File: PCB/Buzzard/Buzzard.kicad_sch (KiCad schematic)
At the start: 71 parts, among them J1 PJ-320A, J4 Haptic Buzz, J5 TrackPoint, J6 OLED, J7 Sharp Memory LCD Breakout, J8 Battery, SW1 SW_DPST_x2, SW2 Reset, U1 ProMicro

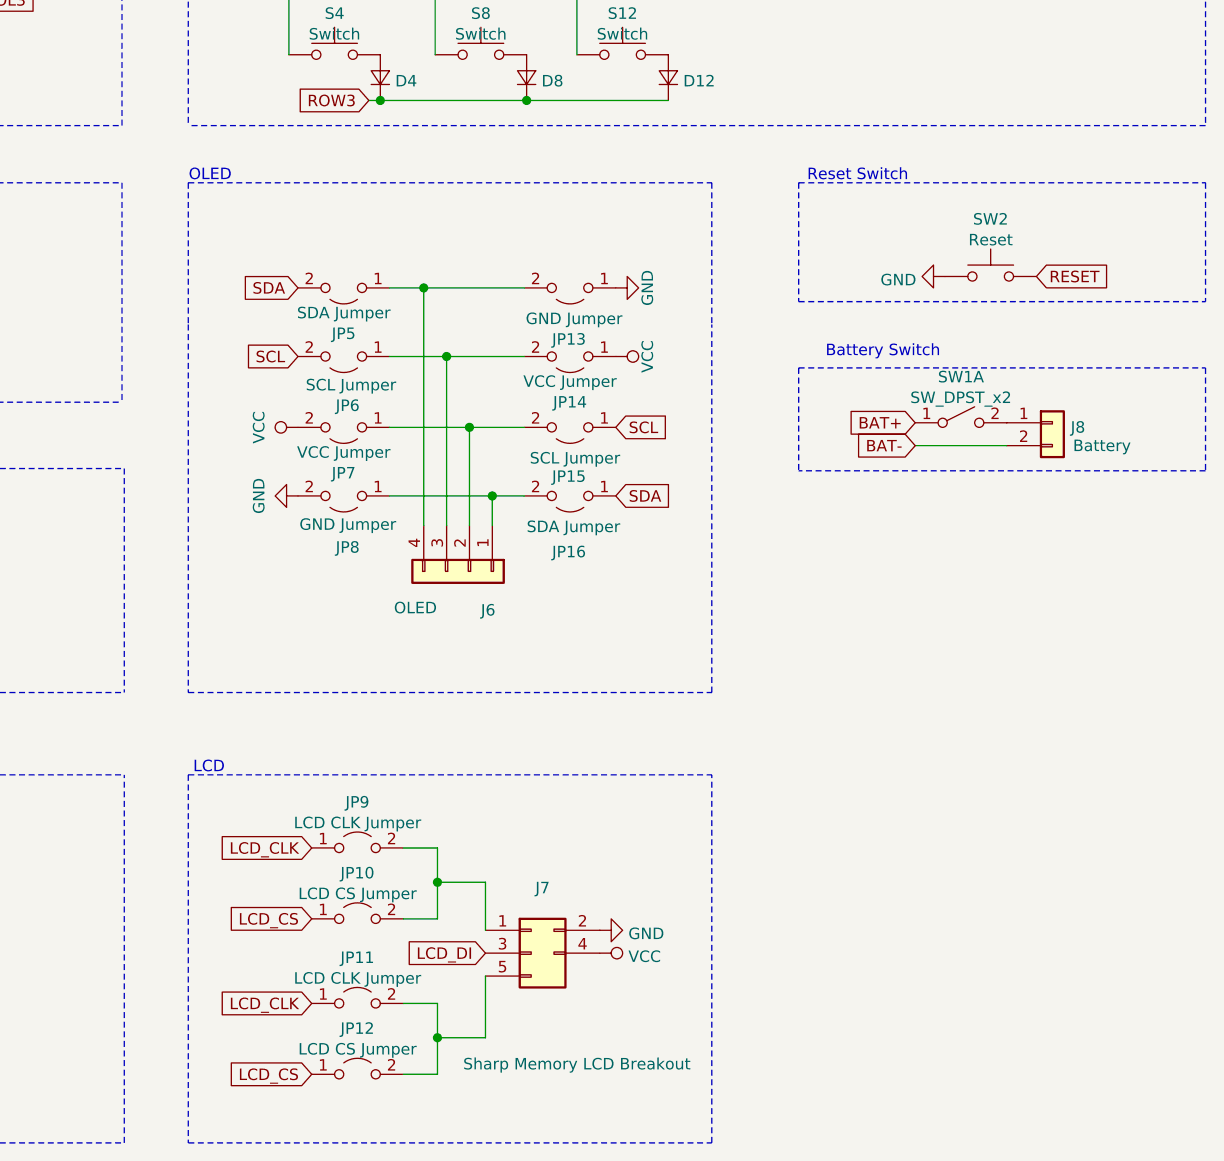
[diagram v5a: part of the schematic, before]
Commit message: replaced lcd footprint and fixed connections
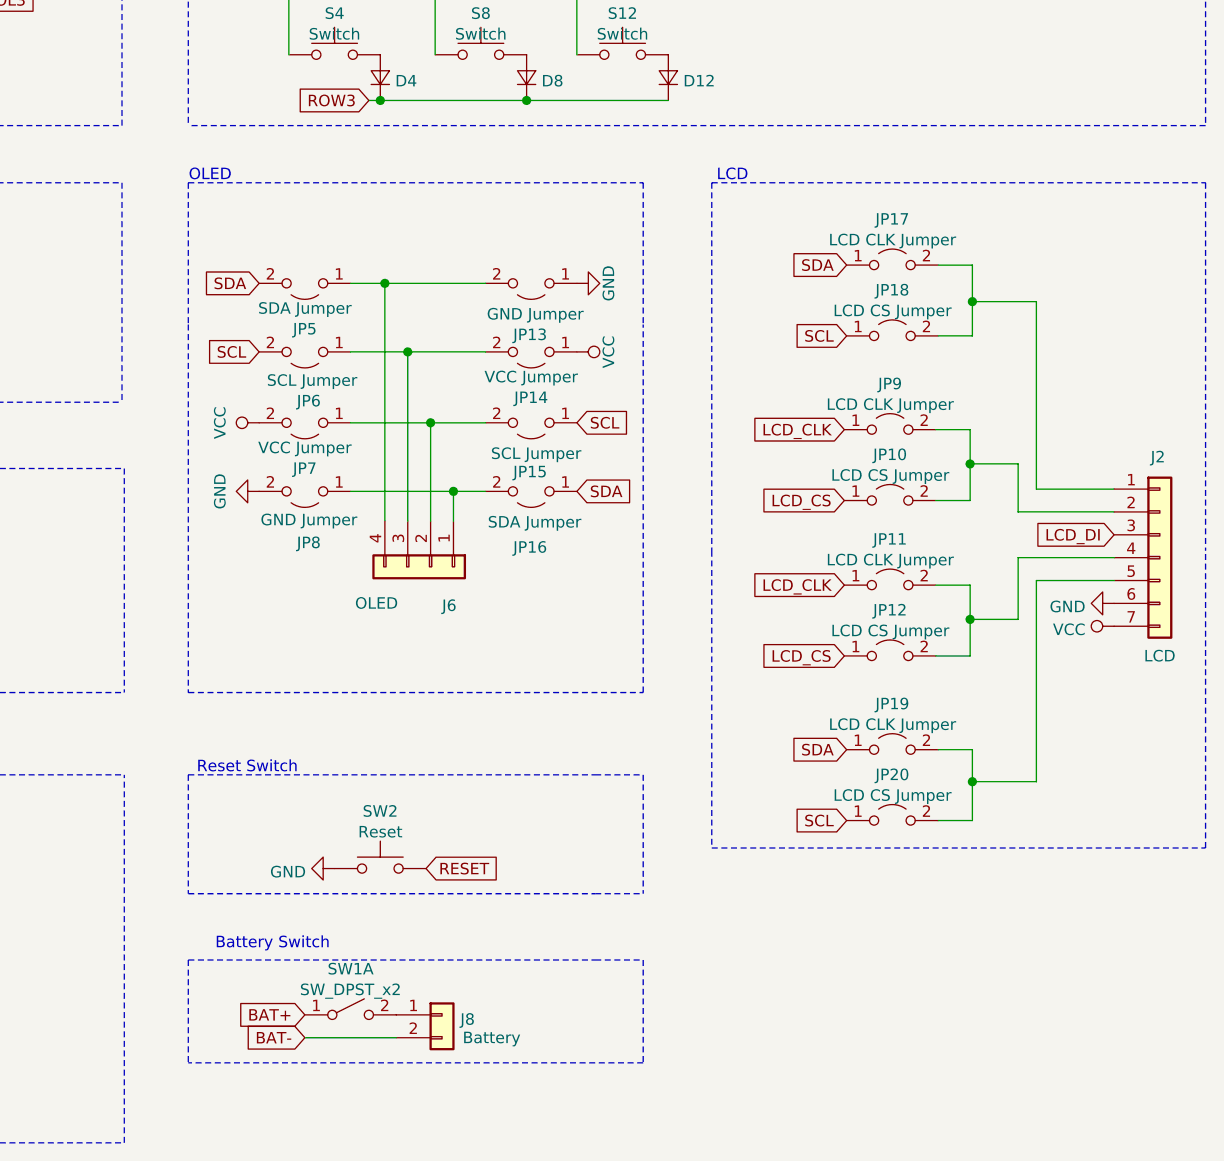
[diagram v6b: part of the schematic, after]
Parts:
- removed J7: Sharp Memory LCD Breakout, Buzzard:SharpMemoryLcdBreakout-Reversable, symbol Connector_Generic:Conn_2Rows-05Pins
- added J2: LCD, Buzzard:SharpMemoryLcdBreakout-Reversable, symbol Connector_Generic:Conn_01x07
- added JP17, JP19: LCD CLK Jumper, Jumper:SolderJumper-2_P1.3mm_Open_Pad1.0x1.5mm, symbol Jumper:Jumper_2_Open
- added JP18, JP20: LCD CS Jumper, Jumper:SolderJumper-2_P1.3mm_Open_Pad1.0x1.5mm, symbol Jumper:Jumper_2_Open
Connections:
- net GND: now also J2.6 (Pin_6)
- net LCD_DI: now also J2.3 (Pin_3)
- net SCL: now also JP18.1 (A), JP20.1 (A)
- net SDA: now also JP17.1 (A), JP19.1 (A)
- net VCC: now also J2.7 (Pin_7)
- net at JP11.2 (B), JP12.2 (B): now also J2.4 (Pin_4)
- net at JP10.2 (B), JP9.2 (B): now also J2.2 (Pin_2)
- new net: J2.1 (Pin_1), JP17.2 (B), JP18.2 (B)
- new net: J2.5 (Pin_5), JP19.2 (B), JP20.2 (B)
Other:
- moved on the sheet: J6, J8, JP10, JP11, JP12, JP13, JP14, JP15, JP16, JP5, JP6, JP7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

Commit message: added mounting holes
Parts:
- added U2, U3: Hole, Buzzard:M2_HOLE_PCB, symbol Buzzard:Hole
- added U4, U5, U6, U7, U8, U9, U? (x4): Hole, Buzzard:HOLE_M2_TH, symbol Buzzard:Hole
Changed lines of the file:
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@@
     (pin "2")
+  )
+  (symbol (lib_id "Buzzard:Hole") (at 240.538 70.612 0) (unit 1)
+    (in_bom yes) (on_board yes) (fields_autoplaced)
+    (property "Reference" "U5" (id 0) (at 244.9831 69.0894 0)
+      (effects (font (size 1.524 1.524)) (justify left))
+    )
+    (property "Value" "Hole" (id 1) (at 244.9831 71.797 0)
+      (effects (font (size 1.524 1.524)) (justify left))
+    )
+    (property "Footprint" "Buzzard:HOLE_M2_TH" (id 2) (at 240.538 70.612 0)
+      (effects (font (size 1.524 1.524)) hide)
+    )
+    (property "Datasheet" "" (id 3) (at 240.538 70.612 0)
+      (effects (font (size 1.524 1.524)))
+    )
+  )
+  (symbol (lib_id "Buzzard:Hole") (at 242.57 116.586 0) (unit 1)
+    (in_bom yes) (on_board yes) (fields_autoplaced)
+    (property "Reference" "U?" (id 0) (at 247.0151 115.0634 0)
+      (effects (font (size 1.524 1.524)) (justify left))
+    )
+    (property "Value" "Hole" (id 1) (at 247.0151 117.771 0)
+      (effects (font (size 1.524 1.524)) (justify left))
+    )
+    (property "Footprint" "Buzzard:HOLE_M2_TH" (id 2) (at 242.57 116.586 0)
+      (effects (font (size 1.524 1.524)) hide)
+    )
+    (property "Datasheet" "" (id 3) (at 242.57 116.586 0)
+      (effects (font (size 1.524 1.524)))
+    )
+  )
+  (symbol (lib_id "Buzzard:Hole") (at 242.824 102.108 0) (unit 1)
+    (in_bom yes) (on_board yes) (fields_autoplaced)
+    (property "Reference" "U?" (id 0) (at 247.2691 100.5854 0)
+      (effects (font (size 1.524 1.524)) (justify left))
+    )
+    (property "Value" "Hole" (id 1) (at 247.2691 103.293 0)
+      (effects (font (size 1.524 1.524)) (justify left))
+    )
+    (property "Footprint" "Buzzard:HOLE_M2_TH" (id 2) (at 242.824 102.108 0)
+      (effects (font (size 1.524 1.524)) hide)
+    )
+    (property "Datasheet" "" (id 3) (at 242.824 102.108 0)
+      (effects (font (size 1.524 1.524)))
+    )
+  )
+  (symbol (lib_id "Buzzard:Hole") (at 243.586 24.384 0) (unit 1)
+    (in_bom yes) (on_board yes) (fields_autoplaced)
+    (property "Reference" "U2" (id 0) (at 248.0311 22.8614 0)
+      (effects (font (size 1.524 1.524)) (justify left))
+    )
+    (property "Value" "Hole" (id 1) (at 248.0311 25.569 0)
+      (effects (font (size 1.524 1.524)) (justify left))
+    )
+    (property "Footprint" "Buzzard:M2_HOLE_PCB" (id 2) (at 243.586 24.384 0)
+      (effects (font (size 1.524 1.524)) hide)
+    )
+    (property "Datasheet" "" (id 3) (at 243.586 24.384 0)
+      (effects (font (size 1.524 1.524)))
+    )
+  )
+  (symbol (lib_id "Buzzard:Hole") (at 243.84 44.704 0) (unit 1)
+    (in_bom yes) (on_board yes) (fields_autoplaced)
+    (property "Reference" "U4" (id 0) (at 248.2851 43.1814 0)
+      (effects (font (size 1.524 1.524)) (justify left))
+    )
+    (property "Value" "Hole" (id 1) (at 248.2851 45.889 0)
+      (effects (font (size 1.524 1.524)) (justify left))
+    )
+    (property "Footprint" "Buzzard:HOLE_M2_TH" (id 2) (at 243.84 44.704 0)
+      (effects (font (size 1.524 1.524)) hide)
+    )
+    (property "Datasheet" "" (id 3) (at 243.84 44.704 0)
+      (effects (font (size 1.524 1.524)))
+    )
+  )
+  (symbol (lib_id "Buzzard:Hole") (at 259.08 70.358 0) (unit 1)
+    (in_bom yes) (on_board yes) (fields_autoplaced)
+    (property "Reference" "U7" (id 0) (at 263.5251 68.8354 0)
+      (effects (font (size 1.524 1.524)) (justify left))
+    )
+    (property "Value" "Hole" (id 1) (at 263.5251 71.543 0)
+      (effects (font (size 1.524 1.524)) (justify left))
+    )
+    (property "Footprint" "Buzzard:HOLE_M2_TH" (id 2) (at 259.08 70.358 0)
+      (effects (font (size 1.524 1.524)) hide)
+    )
+    (property "Datasheet" "" (id 3) (at 259.08 70.358 0)
+      (effects (font (size 1.524 1.524)))
+    )
+  )
+  (symbol (lib_id "Buzzard:Hole") (at 259.842 24.384 0) (unit 1)
+    (in_bom yes) (on_board yes) (fields_autoplaced)
+    (property "Reference" "U3" (id 0) (at 264.2871 22.8614 0)
+      (effects (font (size 1.524 1.524)) (justify left))
+    )
+    (property "Value" "Hole" (id 1) (at 264.2871 25.569 0)
+      (effects (font (size 1.524 1.524)) (justify left))
+    )
+    (property "Footprint" "Buzzard:M2_HOLE_PCB" (id 2) (at 259.842 24.384 0)
+      (effects (font (size 1.524 1.524)) hide)
+    )
+    (property "Datasheet" "" (id 3) (at 259.842 24.384 0)
+      (effects (font (size 1.524 1.524)))
+    )
+  )
+  (symbol (lib_id "Buzzard:Hole") (at 259.842 44.704 0) (unit 1)
+    (in_bom yes) (on_board yes) (fields_autoplaced)
+    (property "Reference" "U6" (id 0) (at 264.2871 43.1814 0)
+      (effects (font (size 1.524 1.524)) (justify left))
+    )
+    (property "Value" "Hole" (id 1) (at 264.2871 45.889 0)
+      (effects (font (size 1.524 1.524)) (justify left))
+    )
+    (property "Footprint" "Buzzard:HOLE_M2_TH" (id 2) (at 259.842 44.704 0)
+      (effects (font (size 1.524 1.524)) hide)
+    )
+    (property "Datasheet" "" (id 3) (at 259.842 44.704 0)
+      (effects (font (size 1.524 1.524)))
+    )
+  )
+  (symbol (lib_id "Buzzard:Hole") (at 261.366 101.092 0) (unit 1)
+    (in_bom yes) (on_board yes) (fields_autoplaced)
+    (property "Reference" "U?" (id 0) (at 265.8111 99.5694 0)
+      (effects (font (size 1.524 1.524)) (justify left))
+    )
+    (property "Value" "Hole" (id 1) (at 265.8111 102.277 0)
+      (effects (font (size 1.524 1.524)) (justify left))
+    )
+    (property "Footprint" "Buzzard:HOLE_M2_TH" (id 2) (at 261.366 101.092 0)
+      (effects (font (size 1.524 1.524)) hide)
+    )
+    (property "Datasheet" "" (id 3) (at 261.366 101.092 0)
+      (effects (font (size 1.524 1.524)))
+    )
+  )
+  (symbol (lib_id "Buzzard:Hole") (at 261.62 116.332 0) (unit 1)
+    (in_bom yes) (on_board yes) (fields_autoplaced)
+    (property "Reference" "U?" (id 0) (at 266.0651 114.8094 0)
+      (effects (font (size 1.524 1.524)) (justify left))
+    )
+    (property "Value" "Hole" (id 1) (at 266.0651 117.517 0)
+      (effects (font (size 1.524 1.524)) (justify left))
+    )
+    (property "Footprint" "Buzzard:HOLE_M2_TH" (id 2) (at 261.62 116.332 0)
+      (effects (font (size 1.524 1.524)) hide)
+    )
+    (property "Datasheet" "" (id 3) (at 261.62 116.332 0)
+      (effects (font (size 1.524 1.524)))
+    )
+  )
+  (symbol (lib_id "Buzzard:Hole") (at 275.082 44.704 0) (unit 1)
+    (in_bom yes) (on_board yes) (fields_autoplaced)
+    (property "Reference" "U8" (id 0) (at 279.5271 43.1814 0)
+      (effects (font (size 1.524 1.524)) (justify left))
+    )
+    (property "Value" "Hole" (id 1) (at 279.5271 45.889 0)
+      (effects (font (size 1.524 1.524)) (justify left))
+    )
+    (property "Footprint" "Buzzard:HOLE_M2_TH" (id 2) (at 275.082 44.704 0)
+      (effects (font (size 1.524 1.524)) hide)
+    )
+    (property "Datasheet" "" (id 3) (at 275.082 44.704 0)
+      (effects (font (size 1.524 1.524)))
+    )
+  )
+  (symbol (lib_id "Buzzard:Hole") (at 277.622 70.104 0) (unit 1)
+    (in_bom yes) (on_board yes) (fields_autoplaced)
+    (property "Reference" "U9" (id 0) (at 282.0671 68.5814 0)
+      (effects (font (size 1.524 1.524)) (justify left))
+    )
+    (property "Value" "Hole" (id 1) (at 282.0671 71.289 0)
+      (effects (font (size 1.524 1.524)) (justify left))
+    )
+    (property "Footprint" "Buzzard:HOLE_M2_TH" (id 2) (at 277.622 70.104 0)
+      (effects (font (size 1.524 1.524)) hide)
+    )
+    (property "Datasheet" "" (id 3) (at 277.622 70.104 0)
+      (effects (font (size 1.524 1.524)))
+    )
   )
   (symbol (lib_id "Connector_Generic:Conn_01x04") (at 140.208 125.984 270) (unit 1)
@@
       (reference "U1") (unit 1) (value "ProMicro") (footprint "Buzzard:ProMicro_v2")
     )
-  )
+    (path "/b10b3035-7c75-4d33-b6a3-e6a3a84e5fd0"
+      (reference "U2") (unit 1) (value "Hole") (footprint "Buzzard:M2_HOLE_PCB")
+    )
+    (path "/bdb675d7-7809-40c3-b4bc-15181b07e6b7"
+      (reference "U3") (unit 1) (value "Hole") (footprint "Buzzard:M2_HOLE_PCB")
+    )
+    (path "/b84c2815-7f12-49e2-a85a-62ab1ffd9d3f"
+      (reference "U4") (unit 1) (value "Hole") (footprint "Buzzard:HOLE_M2_TH")
+    )
+    (path "/42fd8e3f-2892-4411-9954-b309885b7af4"
+      (reference "U5") (unit 1) (value "Hole") (footprint "Buzzard:HOLE_M2_TH")
+    )
+    (path "/17d212a3-6442-413e-b681-d1ce258c7aec"
+      (reference "U6") (unit 1) (value "Hole") (footprint "Buzzard:HOLE_M2_TH")
+    )
+    (path "/635c6e66-34fe-44d5-8653-7dde496ecaec"
+      (reference "U7") (unit 1) (value "Hole") (footprint "Buzzard:HOLE_M2_TH")
+    )
+    (path "/87586d16-3493-4acc-9f40-178b3a129d3b"
+      (reference "U8") (unit 1) (value "Hole") (footprint "Buzzard:HOLE_M2_TH")
+    )
+    (path "/379c27c7-7ded-4ba9-a9cf-2f2156ad142f"
+      (reference "U9") (unit 1) (value "Hole") (footprint "Buzzard:HOLE_M2_TH")
+    )
+    (path "/05302be6-4b7f-4be6-9ed0-2304557fcb76"
+      (reference "U?") (unit 1) (value "Hole") (footprint "Buzzard:HOLE_M2_TH")
+    )
+    (path "/a5b958bb-e9ac-4a1f-be1a-16cf912f3079"
+      (reference "U?") (unit 1) (value "Hole") (footprint "Buzzard:HOLE_M2_TH")
+    )
+    (path "/b276083c-621d-45b3-a26b-cc4498820172"
+      (reference "U?") (unit 1) (value "Hole") (footprint "Buzzard:HOLE_M2_TH")
+    )
+    (path "/ca89250e-33de-4460-9209-96e9c50b09ea"
+      (reference "U?") (unit 1) (value "Hole") (footprint "Buzzard:HOLE_M2_TH")
+    )
+  )

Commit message: diode placement
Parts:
- gave numbers to parts that had none: 4
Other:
- note added: "Holes"
- note added: "Mounting Holes"
- note added: "Shield"
- moved on the sheet: U10, U11, U12, U13, U2, U3, U4, U5, U6, U7, U8, U9
